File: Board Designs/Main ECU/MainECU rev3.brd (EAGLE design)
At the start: 120.6 x 78.9 mm, 148 parts, among them X1 CONNECTOR-37, X2 CONNECTOR-4AUTOSPORT, X3 CONNECTOR-4NANO-FIT-VERTICAL-4, X4 CONNECTOR-4NANO-FIT-VERTICAL-4

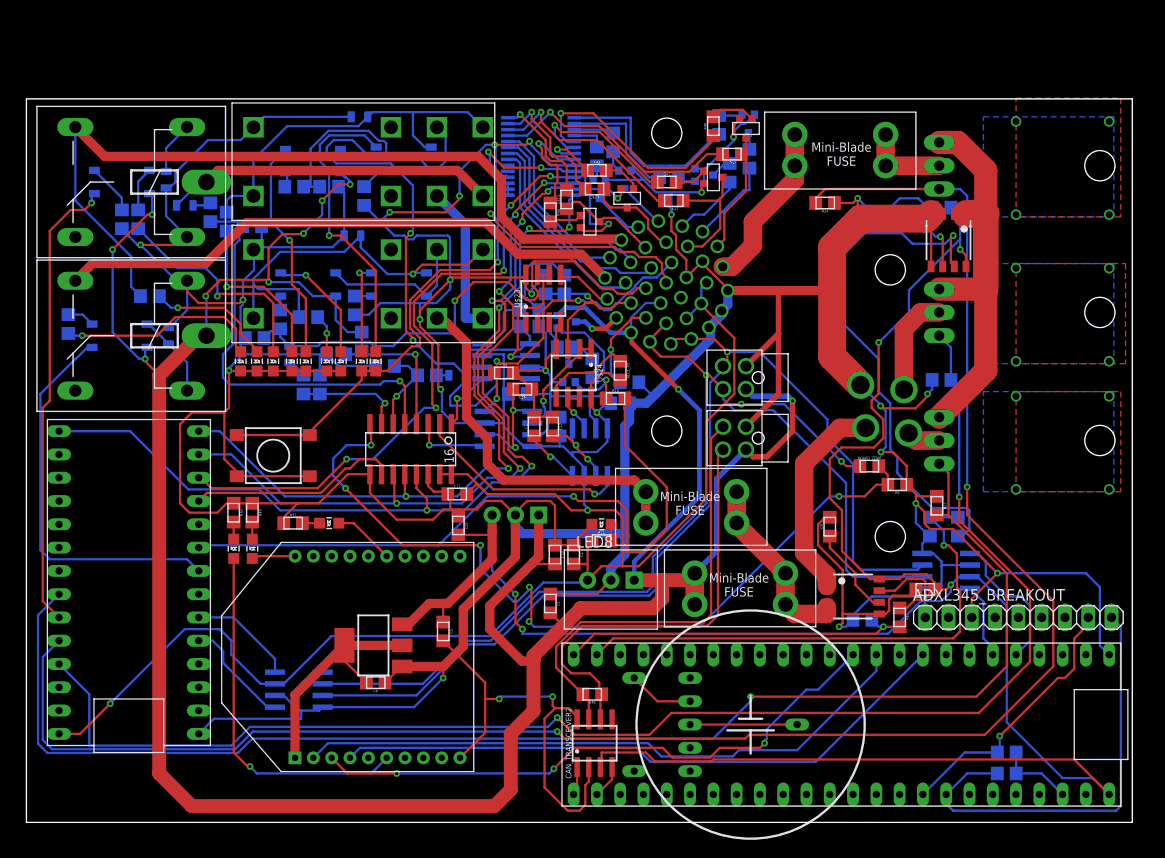
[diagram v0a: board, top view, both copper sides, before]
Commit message: MainECU rev3: Move RTC battery to within board footprint, update XBee package size, add SPI level shifter, Add mosfet drivers and zener diodes, Replace relay control SSRs with transistors
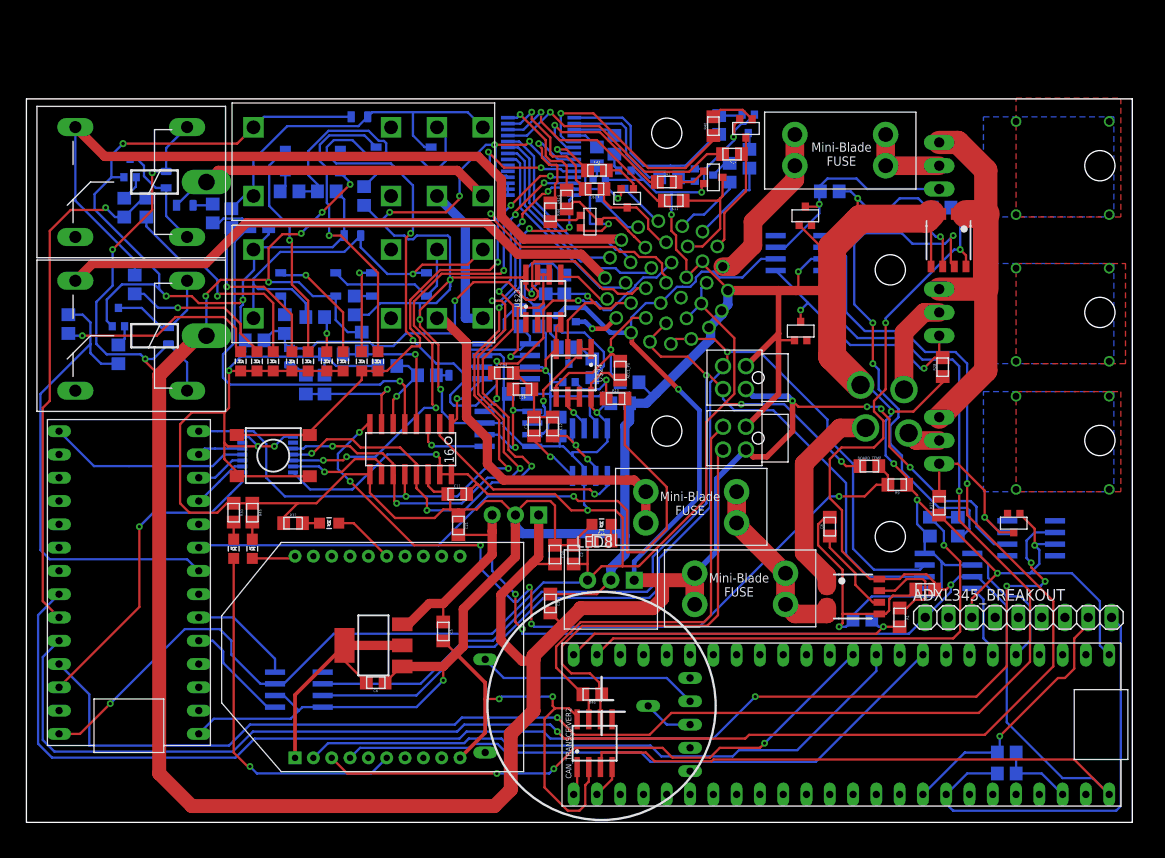
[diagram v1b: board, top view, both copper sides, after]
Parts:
- removed INVERTER_SSR: CPC1002N, HyTechDevices:SOP04
- removed R25: 330, HyTechDevices:0805
- added D7, D8, D9: MMBZ5246BLT1G, HyTechDevices:SOT23
- added Q11, Q9: MMBT3904LT3G, HyTechDevices:SOT23
- added R47, R50: 2.2k, HyTechDevices:0805
- added U$19: MC34152, HyTechDevices:SOIC-08
- added U$25: TXB0104TSSOP, HyTechDevices:TSSOP-14
- Q1, Q2, Q3, Q4, Q5, Q6, Q7, Q8: value (none) -> MMBT3904LT3G
- R16: value 43 -> 100
- U$4, U$6, U$7: value N-CHANNEL_MOSFET_HOR_HOLE -> N-CHANNEL_MOSFET_FQP30N06L
- U$5: value CPC1002N -> MC34152; device HyTechDevices:SOP04 -> HyTechDevices:SOIC-08
- moved U$5 74.3 mm to (84.3, 62.1), turned to 270 degrees
- moved U$16 16.4 mm to (62.7, 12.7)
- moved R31 2.08 mm to (11.8, 58.7), turned to 270 degrees
- moved R26 1.55 mm to (13.1, 67.1)
- moved R28 1.40 mm to (99.9, 49.7), flipped to the top, turned to 90 degrees
- moved R24 1.37 mm to (87.6, 68.8), flipped to the bottom, turned to 0 degrees
- moved R14 0.76 mm to (31.5, 55.1)
- moved R22 0.76 mm to (25.4, 65.0)
- moved R11 0.72 mm to (28.7, 68.8)
- moved R21 0.72 mm to (28.2, 54.4)
- moved R17 0.63 mm to (22.4, 65.9)
- moved R19 0.57 mm to (32.8, 68.8)
- moved R6 0.51 mm to (32.5, 47.8)
- moved R38 0.28 mm to (64.1, 73.9)
- moved R15 0.28 mm to (20.3, 66.4)
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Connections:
- removed net CHIP_SELECT1: U$1.D9(RX2), U$18.10
- removed net CHIP_SELECT2: U$1.D10(TX2), U$17.11
- removed net N$43: D10.C, R26.1, SOFTWARE_SHUTOFF.2, U$5.3
- removed net N$44: R25.2, U$5.2
- new net 3.3V_MAIN_TEENSY: U$1.3.3V, U$25.1
- new net CS1_5V: U$18.10, U$25.13
- new net CS1_TEENSY: U$1.D9(RX2), U$25.2
- new net CS2_5V: U$17.11, U$25.12
- new net CS2_TEENSY: U$1.D10(TX2), U$25.3
- new net FAN1DRIVE: D8.3, R24.2, U$5.7, U$7.1
- new net FAN2DRIVE: D7.3, R28.2, U$4.1, U$5.5
- new net MOSI_5V: U$17.13, U$18.11, U$25.10
- new net N$65: Q9.1, R47.2
- new net N$66: D4.A, Q9.3, U$8.2
- new net PUMPDRIVE: D9.3, R27.2, U$19.7, U$6.1
- new net SCK_5V: U$17.12, U$18.13, U$25.11
- net +12V: now also D10.C, D4.C, SOFTWARE_SHUTOFF.2, U$19.6, U$5.6, U$8.1; no longer INVERTER_SSR.4, U$5.4
- net +5V: now also U$25.14
- net FAN1CONTROL: now also U$5.2; no longer R24.2, U$7.1
- net FAN2CONTROL: now also U$5.4; no longer R28.2, U$4.1
- net GND: now also D7.1, D8.1, D9.1, Q11.2, Q9.2, U$19.3, U$25.7, U$25.8, U$5.3; no longer D10.A, D4.A, R25.1, SOFTWARE_SHUTOFF.1, U$8.2
- net INVERTER_CTRL: now also R16.1, R47.1; no longer INVERTER_SSR.1
- net MOSI_TEENSY: now also U$25.5; no longer U$17.13, U$18.11
- net N$26: now also Q11.1, R50.2; no longer D4.C, INVERTER_SSR.3, U$8.1
- net N$27: now also D10.A, Q11.3, SOFTWARE_SHUTOFF.1; no longer INVERTER_SSR.2, R16.1
- net PUMPCONTROL: now also U$19.2; no longer R27.2, U$6.1
- net SCK_TEENSY: now also U$25.4; no longer U$17.12, U$18.13
- net SOFTWARE_SHUTDOWN: now also R26.1, R50.1; no longer U$5.1
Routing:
- net SCK_TEENSY: track 102.5 -> 22.1 mm, vias 5 -> 0
- net MOSI_TEENSY: track 83.1 -> 5.01 mm, vias 5 -> 0
- net SCK_5V: track 0.00 -> 75.2 mm, vias 0 -> 6
- net MOSI_5V: track 0.00 -> 72.2 mm, vias 0 -> 6
- net CHIP_SELECT2: track 69.5 -> 0.00 mm, vias 5 -> 0
- net +12V: track 315.0 -> 381.7 mm, vias 10 -> 13
- net CS2_5V: track 0.00 -> 57.5 mm, vias 0 -> 6
- net 3.3V_MAIN_TEENSY: track 0.00 -> 35.4 mm, vias 0 -> 1
- net GND: track 739.3 -> 774.4 mm, vias 21 -> 25
- net FAN2DRIVE: track 0.00 -> 28.1 mm, vias 0 -> 2
- net FAN1DRIVE: track 0.00 -> 24.8 mm, vias 0 -> 1
- net CHIP_SELECT1: track 23.1 -> 0.00 mm
- net +5V: track 317.3 -> 337.4 mm, vias 13 -> 14
- net PUMPDRIVE: track 0.00 -> 19.6 mm, vias 0 -> 1
- net N$60: track 7.15 -> 24.2 mm
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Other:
- board text added: "Designed by Parker Jones"
- board text added: "HyTech 2019 Main ECU rev3"
- board text added: "Shutdown Latch"
- board text added: "Updates by Nathan Cheek"
- board text removed: "Designed By Parker Jones"
- board text removed: "HyTech 2019 Main ECU rev2"

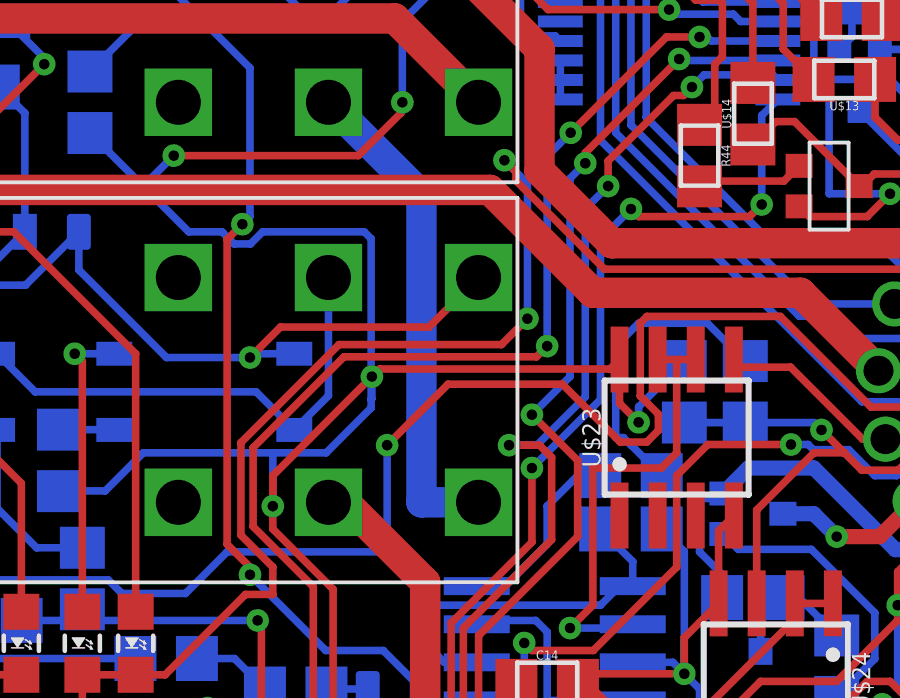
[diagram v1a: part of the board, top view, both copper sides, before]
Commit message: Main ECU: [rev2, rev3] Fix filter frequency capacitor values, [rev1b, rev3] shorten a few traces
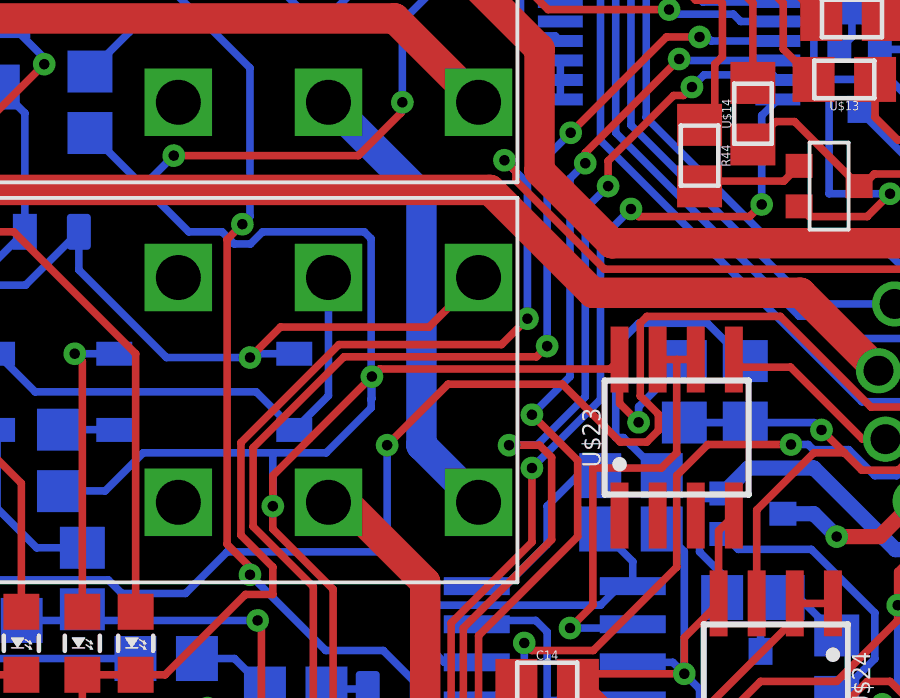
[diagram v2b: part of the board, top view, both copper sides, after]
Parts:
- C14, C17, C3: value 5.3uF -> 47pF
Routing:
- net SHUTDOWN_B: track 16.5 -> 15.4 mm
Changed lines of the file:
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@@
 <attribute name="VALUE" x="64.008" y="40.386" size="0.6096" layer="28" rot="MR90" align="bottom-center"/>
 </element>
-<element name="C3" library="HyTechDevices" package="0805" value="5.3uF" x="55.372" y="43.18" smashed="yes" rot="R90">
+<element name="C3" library="HyTechDevices" package="0805" value="47pF" x="55.372" y="43.18" smashed="yes" rot="R90">
 <attribute name="NAME" x="54.6481" y="43.18" size="0.3048" layer="25" rot="R90" align="bottom-center"/>
 <attribute name="VALUE" x="56.0832" y="43.18" size="0.3048" layer="27" rot="R90" align="top-center"/>
@@
 <attribute name="VALUE" x="52.578" y="40.386" size="0.6096" layer="28" rot="MR180" align="bottom-center"/>
 </element>
-<element name="C14" library="HyTechDevices" package="0805" value="5.3uF" x="52.07" y="49.022" smashed="yes">
+<element name="C14" library="HyTechDevices" package="0805" value="47pF" x="52.07" y="49.022" smashed="yes">
 <attribute name="NAME" x="52.07" y="49.7459" size="0.3048" layer="25" align="bottom-center"/>
 </element>
@@
 <attribute name="VALUE" x="52.324" y="47.752" size="0.6096" layer="28" rot="MR180" align="bottom-center"/>
 </element>
-<element name="C17" library="HyTechDevices" package="0805" value="5.3uF" x="54.864" y="55.88" smashed="yes" rot="MR180">
+<element name="C17" library="HyTechDevices" package="0805" value="47pF" x="54.864" y="55.88" smashed="yes" rot="MR180">
 <attribute name="NAME" x="54.864" y="55.1561" size="0.3048" layer="26" rot="MR180" align="bottom-center"/>
 <attribute name="VALUE" x="54.864" y="56.5912" size="0.3048" layer="28" rot="MR180" align="top-center"/>
@@
 <contactref element="IMD_SHUTDOWN" pad="5"/>
 <wire x1="47.879" y1="65.2272" x2="44.7802" y2="68.326" width="1.016" layer="16"/>
-<wire x1="47.879" y1="54.991" x2="47.879" y2="65.2272" width="1.016" layer="16"/>
-<wire x1="49.784" y1="54.991" x2="47.879" y2="54.991" width="1.016" layer="16"/>
+<wire x1="47.879" y1="56.896" x2="47.879" y2="65.2272" width="1.016" layer="16"/>
+<wire x1="49.784" y1="54.991" x2="47.879" y2="56.896" width="1.016" layer="16"/>
 </signal>
 <signal name="N$32">
